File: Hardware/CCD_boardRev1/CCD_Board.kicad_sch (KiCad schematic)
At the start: 12 parts, among them Q1 Q_PNP_ECB, U1 74AHC04, U2 TCD1304

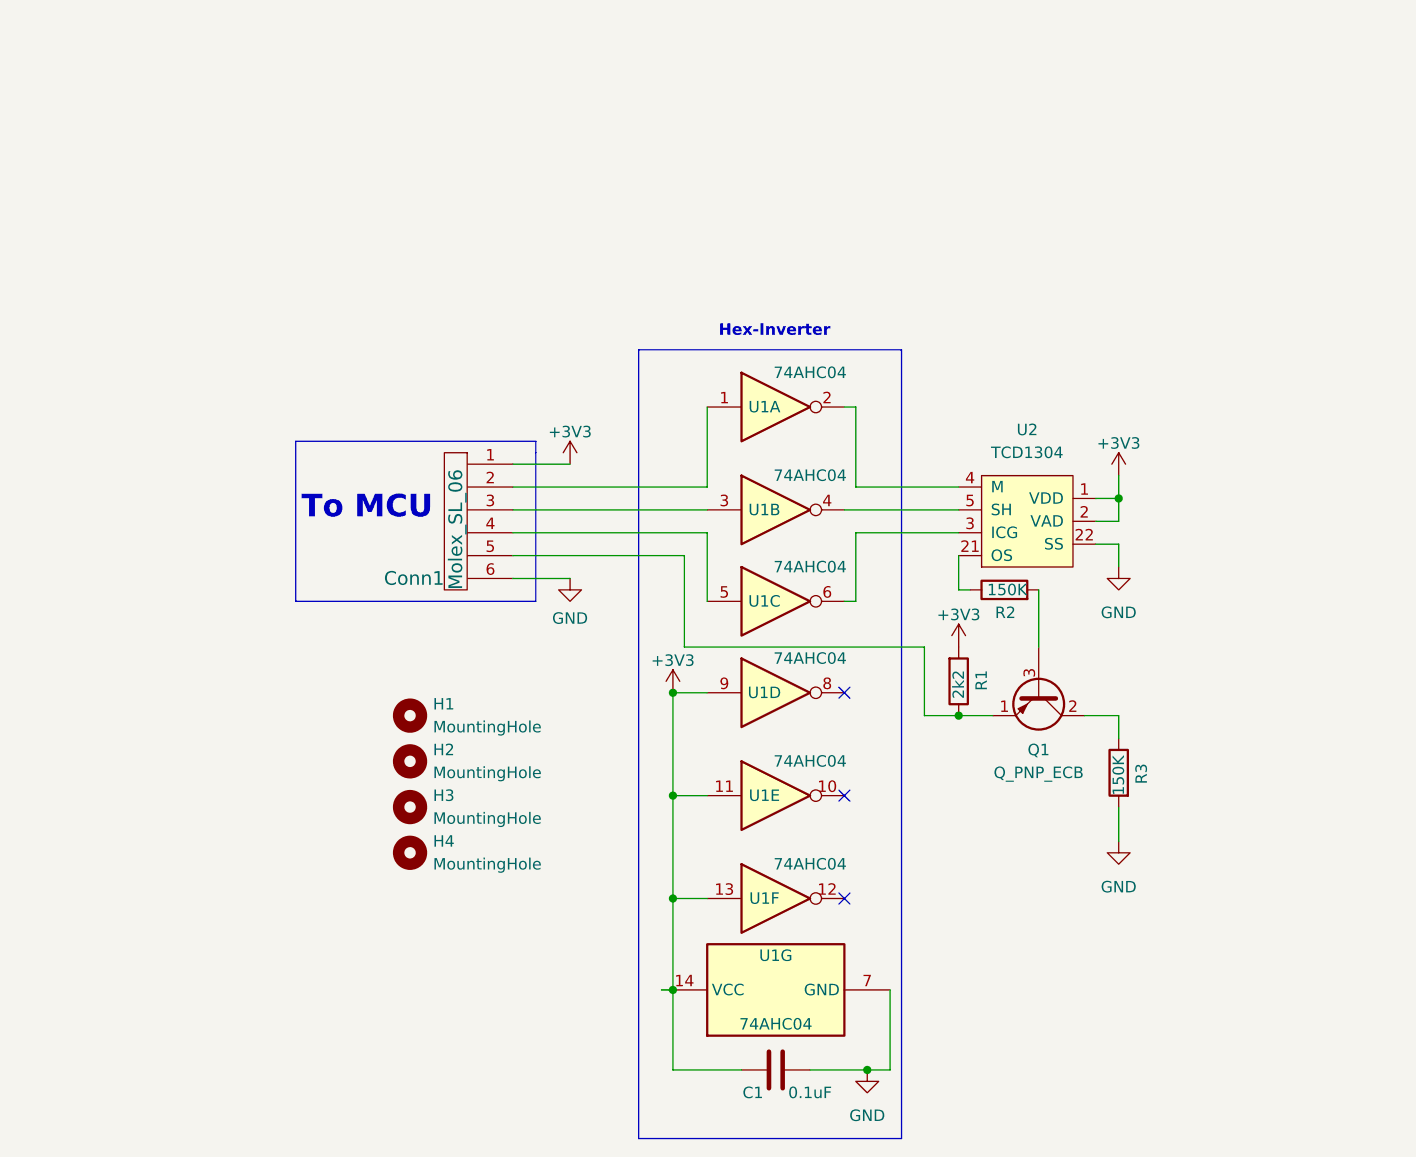
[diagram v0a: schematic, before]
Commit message: page edits for printing
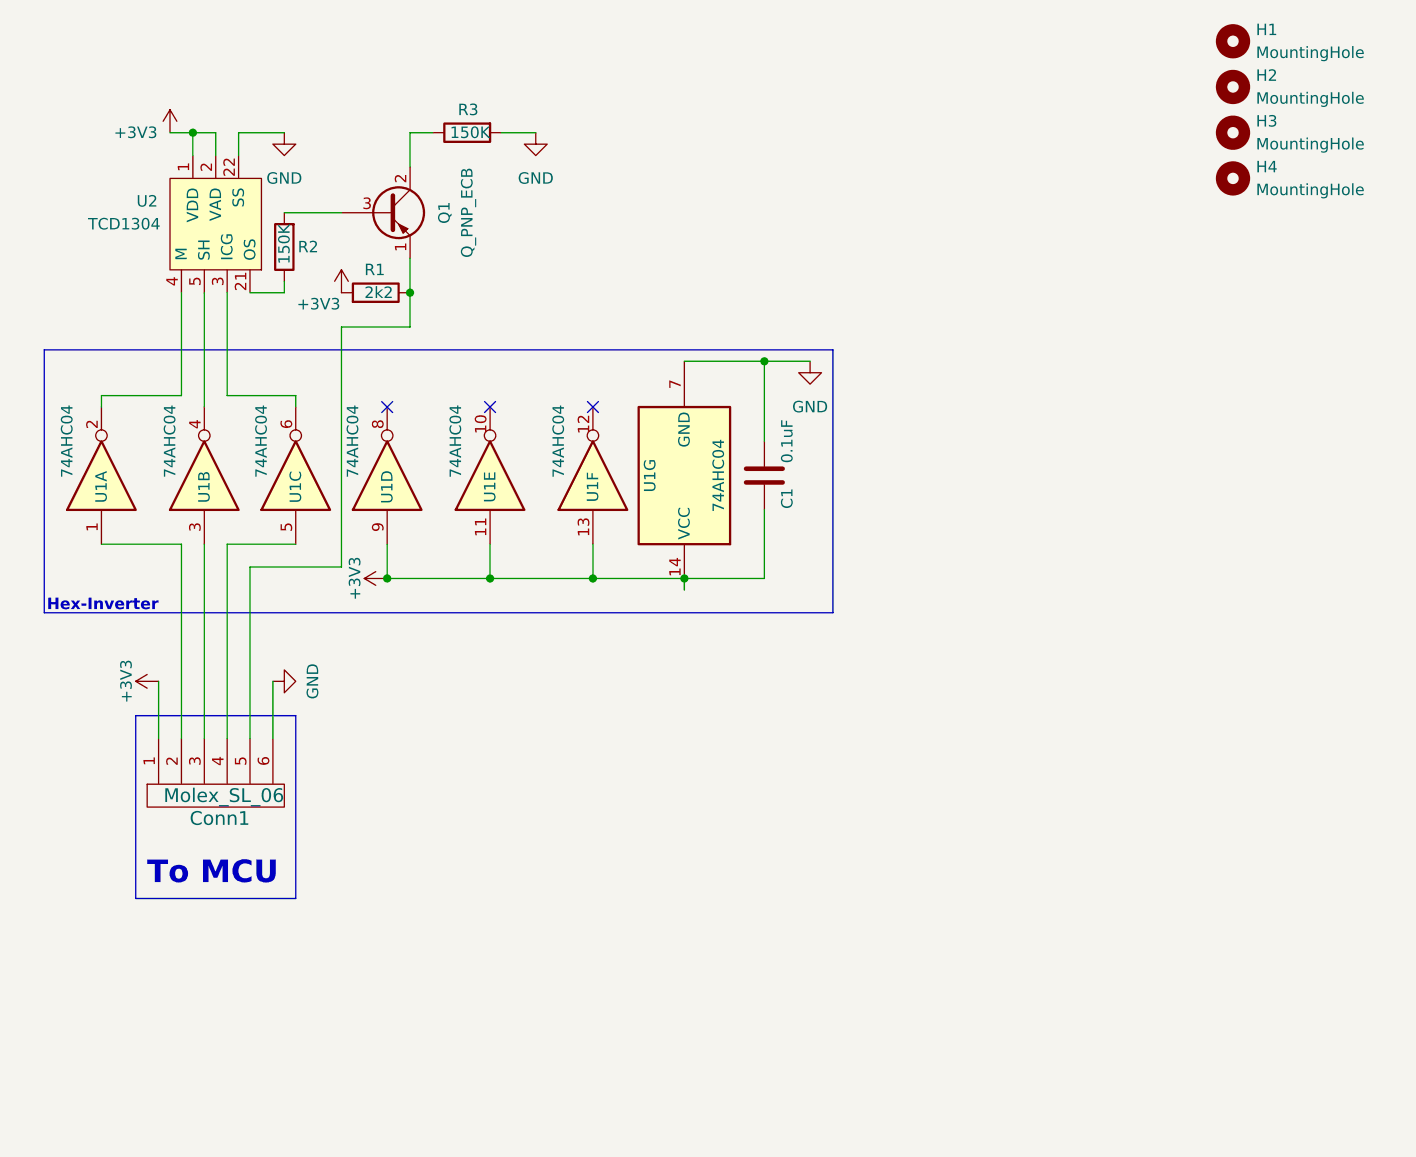
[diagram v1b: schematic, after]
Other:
- company: (none) -> MRDT
- title: (none) -> CCD Board
- moved on the sheet: C1, Conn1, H1, H2, H3, H4, Q1, R1, R2, R3, U1A, U1B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
